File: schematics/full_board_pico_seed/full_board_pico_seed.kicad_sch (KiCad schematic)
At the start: 31 parts, among them J10 Conn_02x20_Odd_Even, J2 Conn_01x02_Male, J9 Conn_01x03, P0 25k, P1 25k, P2 25k, SW4 Enter, SW5 Exit, U12 128X64 OLED Display, U14 AP63205WU, U3 LM1117DT-5.0

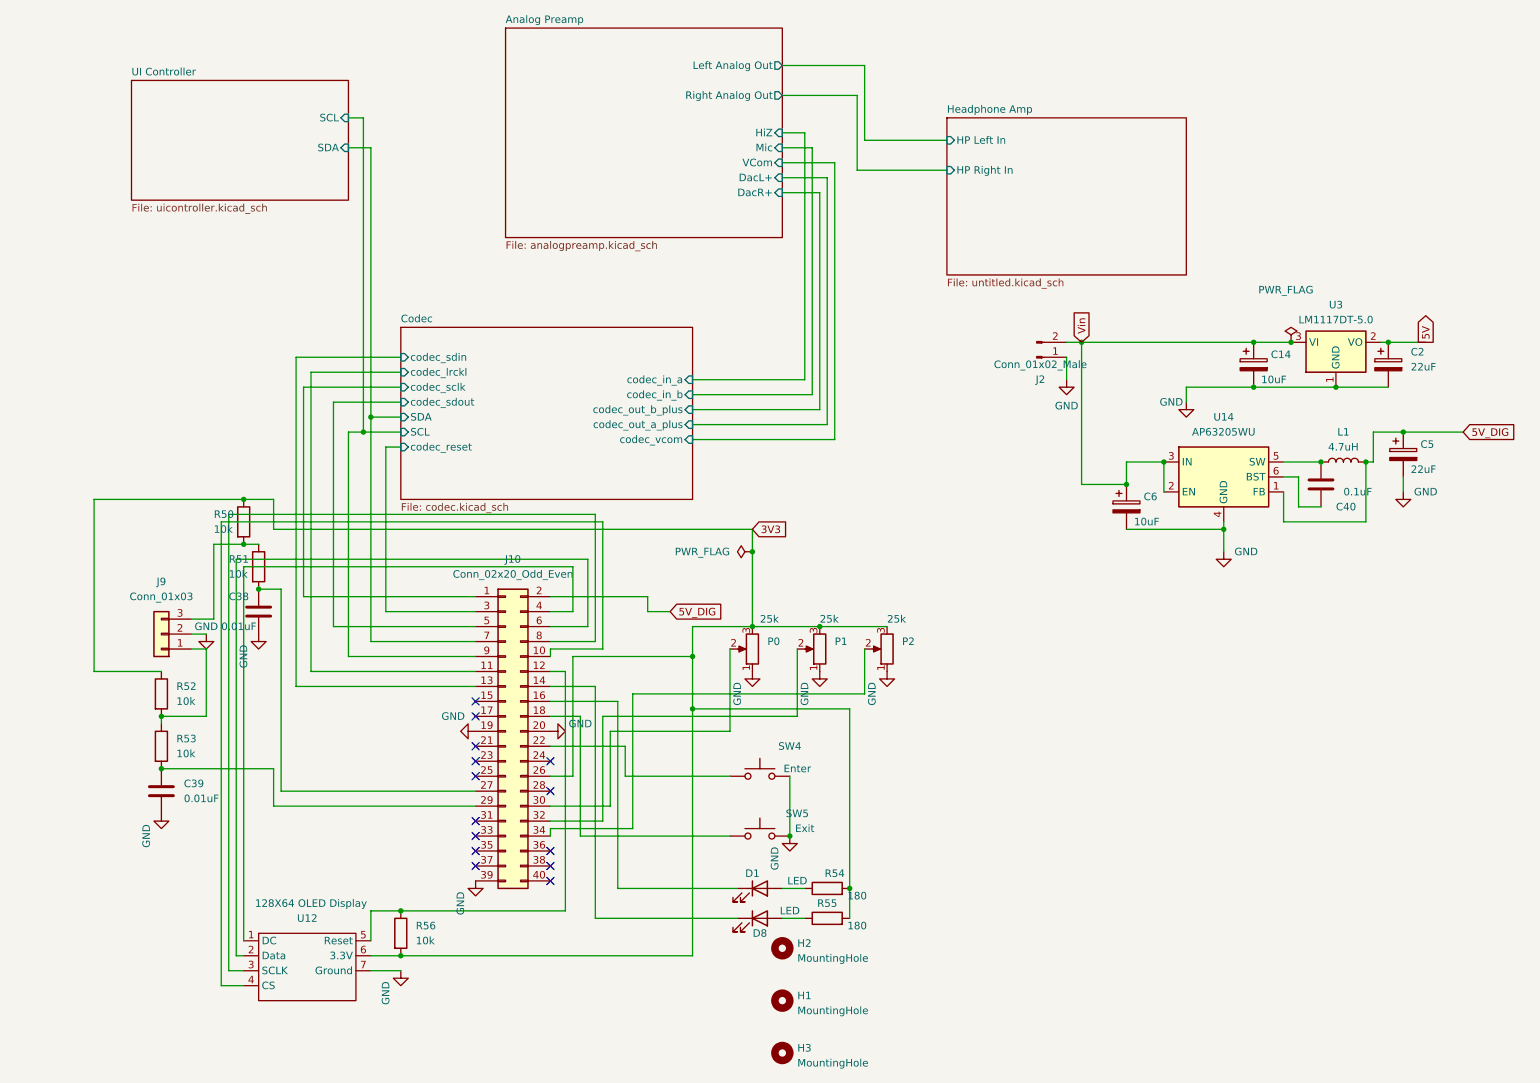
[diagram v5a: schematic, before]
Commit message: corrected schematic regarding pcm3060
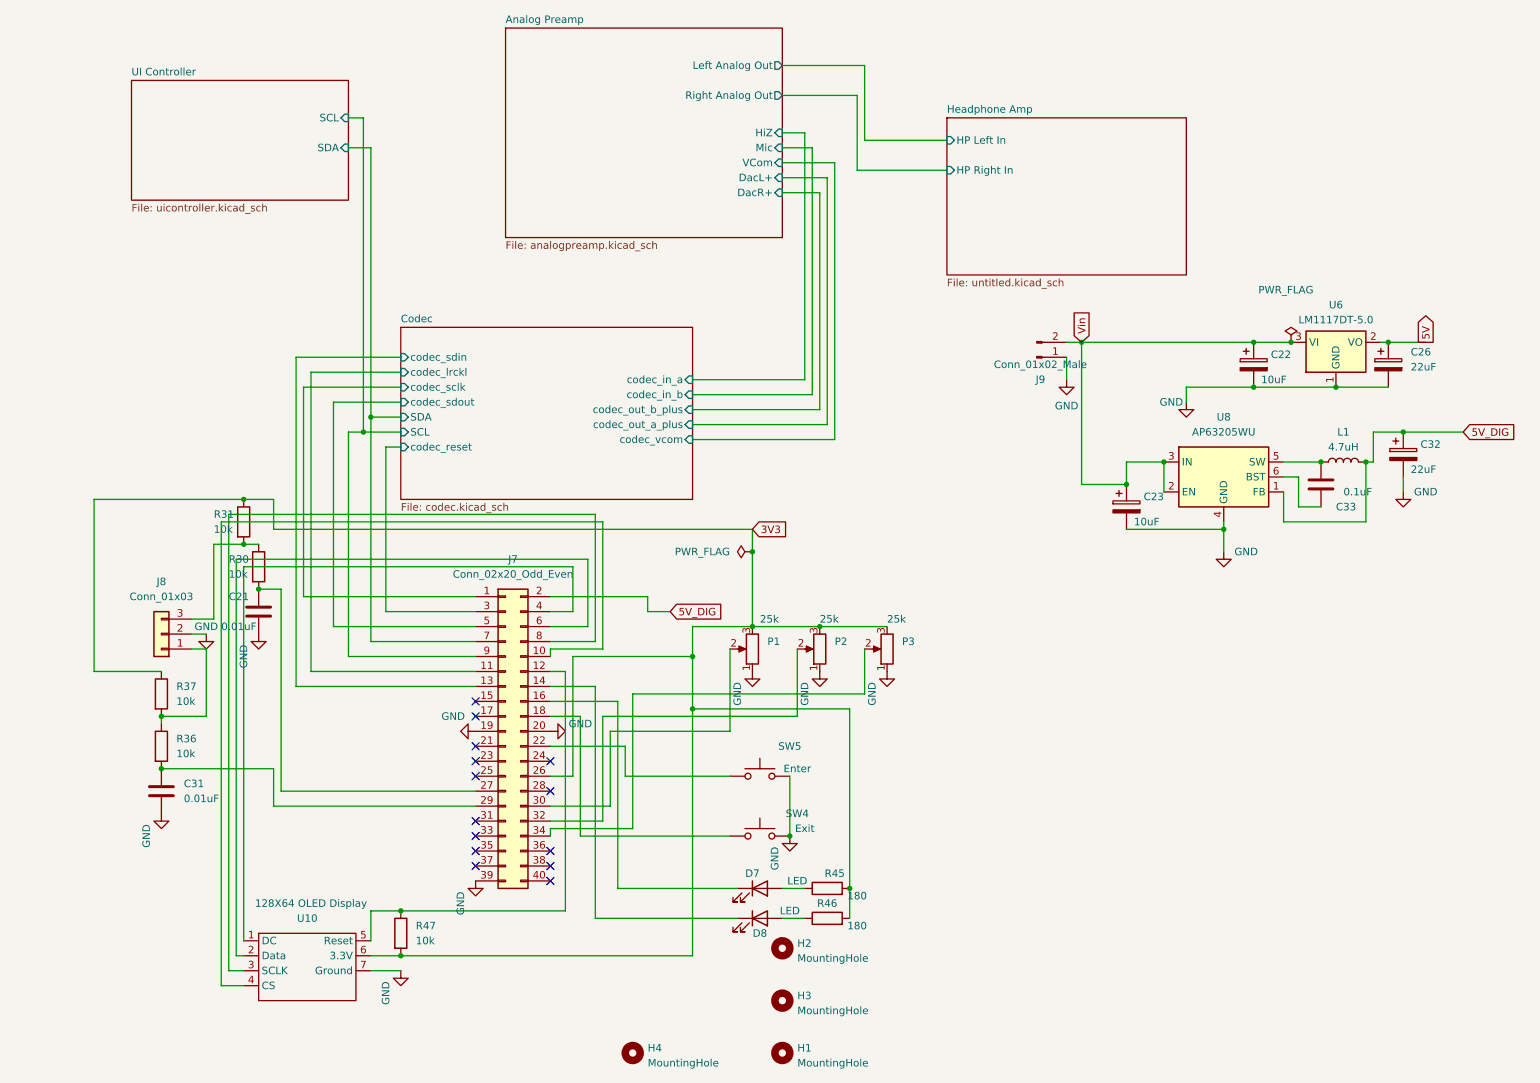
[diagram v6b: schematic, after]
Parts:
- added H4: MountingHole, MountingHole:MountingHole_3.2mm_M3, symbol Mechanical:MountingHole
- renumbered C38 to C21, C14 to C22, C6 to C23, C2 to C26, C39 to C31, C5 to C32, C40 to C33, D1 to D7, H3 to H1, H1 to H3, J10 to J7, J9 to J8, J2 to J9, P0 to P1, P1 to P2, P2 to P3, R51 to R30, R50 to R31, R53 to R36, R52 to R37, R54 to R45, R55 to R46, R56 to R47, SW5 to SW4, SW4 to SW5, U12 to U10, U3 to U6, U14 to U8
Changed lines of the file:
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@@
 	)
 	(symbol
+		(lib_id "Mechanical:MountingHole")
+		(at 132.08 193.04 0)
+		(unit 1)
+		(exclude_from_sim no)
+		(in_bom no)
+		(on_board yes)
+		(dnp no)
+		(fields_autoplaced yes)
+		(property "Reference" "H4"
+			(at 134.62 192.2053 0)
+			(effects
+				(font
+					(size 1.27 1.27)
+				)
+				(justify left)
+			)
+		)
+		(property "Value" "MountingHole"
+			(at 134.62 194.7422 0)
+			(effects
+				(font
+					(size 1.27 1.27)
+				)
+				(justify left)
+			)
+		)
+		(property "Footprint" "MountingHole:MountingHole_3.2mm_M3"
+			(at 132.08 193.04 0)
+			(effects
+				(font
+					(size 1.27 1.27)
+				)
+				(hide yes)
+			)
+		)
+		(property "Datasheet" "~"
+			(at 132.08 193.04 0)
+			(effects
+				(font
+					(size 1.27 1.27)
+				)
+				(hide yes)
+			)
+		)
+		(property "Description" ""
+			(at 132.08 193.04 0)
+			(effects
+				(font
+					(size 1.27 1.27)
+				)
+				(hide yes)
+			)
+		)
+		(instances
+			(project "full_board_pico_seed"
+				(path "/e63e39d7-6ac0-4ffd-8aa3-1841a4541b55"
+					(reference "H4")
+					(unit 1)
+				)
+			)
+		)
+	)
+	(symbol
 		(lib_id "power:GND")
 		(at 105.41 163.83 0)
@@
 		(on_board yes)
 		(dnp no)
-		(property "Reference" "R51"
+		(property "Reference" "R30"
 			(at 63.5 109.22 0)
 			(effects
@@
 			(project "full_board_pico_seed"
 				(path "/e63e39d7-6ac0-4ffd-8aa3-1841a4541b55"
-					(reference "R51")
+					(reference "R30")
 					(unit 1)
 				)
@@
 		(on_board yes)
 		(dnp no)
-		(property "Reference" "P0"
+		(property "Reference" "P1"
 			(at 154.94 123.19 0)
 			(effects
@@
 			(project "full_board_pico_seed"
 				(path "/e63e39d7-6ac0-4ffd-8aa3-1841a4541b55"
-					(reference "P0")
+					(reference "P1")
 					(unit 1)
 				)
@@
 		(dnp no)
 		(fields_autoplaced yes)
-		(property "Reference" "C39"
+		(property "Reference" "C31"
 			(at 55.88 147.32 0)
 			(effects
@@
 			(project "full_board_pico_seed"
 				(path "/e63e39d7-6ac0-4ffd-8aa3-1841a4541b55"
-					(reference "C39")
+					(reference "C31")
 					(unit 1)
 				)
@@
 		(on_board yes)
 		(dnp no)
-		(property "Reference" "P1"
+		(property "Reference" "P2"
 			(at 166.37 123.19 0)
 			(effects
@@
 			(project "full_board_pico_seed"
 				(path "/e63e39d7-6ac0-4ffd-8aa3-1841a4541b55"
-					(reference "P1")
+					(reference "P2")
 					(unit 1)
 				)
@@
 		(dnp no)
 		(fields_autoplaced yes)
-		(property "Reference" "R52"
+		(property "Reference" "R37"
 			(at 54.61 130.81 0)
 			(effects
@@
 			(project "full_board_pico_seed"
 				(path "/e63e39d7-6ac0-4ffd-8aa3-1841a4541b55"
-					(reference "R52")
+					(reference "R37")
 					(unit 1)
 				)
@@
 		(dnp no)
 		(fields_autoplaced yes)
-		(property "Reference" "R56"
+		(property "Reference" "R47"
 			(at 95.25 171.45 0)
 			(effects
@@
 			(project "full_board_pico_seed"
 				(path "/e63e39d7-6ac0-4ffd-8aa3-1841a4541b55"
-					(reference "R56")
+					(reference "R47")
 					(unit 1)
 				)
@@
 		(on_board yes)
 		(dnp no)
-		(property "Reference" "C38"
+		(property "Reference" "C21"
 			(at 63.5 115.57 0)
 			(effects
@@
 			(project "full_board_pico_seed"
 				(path "/e63e39d7-6ac0-4ffd-8aa3-1841a4541b55"
-					(reference "C38")
+					(reference "C21")
 					(unit 1)
 				)
@@
 		(dnp no)
 		(fields_autoplaced yes)
-		(property "Reference" "R53"
+		(property "Reference" "R36"
 			(at 54.61 139.7 0)
 			(effects
@@
 			(project "full_board_pico_seed"
 				(path "/e63e39d7-6ac0-4ffd-8aa3-1841a4541b55"
-					(reference "R53")
+					(reference "R36")
 					(unit 1)
 				)
@@
 		(on_board yes)
 		(dnp no)
-		(property "Reference" "SW5"
+		(property "Reference" "SW4"
 			(at 160.02 152.4 0)
 			(effects
@@
 			(project "full_board_pico_seed"
 				(path "/e63e39d7-6ac0-4ffd-8aa3-1841a4541b55"
-					(reference "SW5")
+					(reference "SW4")
 					(unit 1)
 				)
@@
 		(on_board yes)
 		(dnp no)
-		(property "Reference" "C14"
+		(property "Reference" "C22"
 			(at 240.411 74.4763 0)
 			(effects
@@
 			(project "full_board_pico_seed"
 				(path "/e63e39d7-6ac0-4ffd-8aa3-1841a4541b55"
-					(reference "C14")
+					(reference "C22")
 					(unit 1)
 				)
@@
 		(dnp no)
 		(fields_autoplaced yes)
-		(property "Reference" "H1"
+		(property "Reference" "H3"
 			(at 160.02 183.3153 0)
 			(effects
@@
 			(project "full_board_pico_seed"
 				(path "/e63e39d7-6ac0-4ffd-8aa3-1841a4541b55"
-					(reference "H1")
+					(reference "H3")
 					(unit 1)
 				)
@@
 		(on_board yes)
 		(dnp no)
-		(property "Reference" "C5"
+		(property "Reference" "C32"
 			(at 265.811 89.7163 0)
 			(effects
@@
 			(project "full_board_pico_seed"
 				(path "/e63e39d7-6ac0-4ffd-8aa3-1841a4541b55"
-					(reference "C5")
+					(reference "C32")
 					(unit 1)
 				)
@@
 		(on_board yes)
 		(dnp no)
-		(property "Reference" "J2"
+		(property "Reference" "J9"
 			(at 201.295 78.706 0)
 			(effects
@@
 			(project "full_board_pico_seed"
 				(path "/e63e39d7-6ac0-4ffd-8aa3-1841a4541b55"
-					(reference "J2")
+					(reference "J9")
 					(unit 1)
 				)
@@
 		(dnp no)
 		(fields_autoplaced yes)
-		(property "Reference" "U3"
+		(property "Reference" "U6"
 			(at 251.46 66.04 0)
 			(effects
@@
 			(project "full_board_pico_seed"
 				(path "/e63e39d7-6ac0-4ffd-8aa3-1841a4541b55"
-					(reference "U3")
+					(reference "U6")
 					(unit 1)
 				)
@@
 		(on_board yes)
 		(dnp no)
-		(property "Reference" "R50"
+		(property "Reference" "R31"
 			(at 60.96 101.6 0)
 			(effects
@@
 			(project "full_board_pico_seed"
 				(path "/e63e39d7-6ac0-4ffd-8aa3-1841a4541b55"
-					(reference "R50")
+					(reference "R31")
 					(unit 1)
 				)
@@
 		(on_board yes)
 		(dnp no)
-		(property "Reference" "C40"
+		(property "Reference" "C33"
 			(at 251.46 100.33 0)
 			(effects
@@
 			(project "full_board_pico_seed"
 				(path "/e63e39d7-6ac0-4ffd-8aa3-1841a4541b55"
-					(reference "C40")
+					(reference "C33")
 					(unit 1)
 				)
@@
 		(on_board yes)
 		(dnp no)
-		(property "Reference" "SW4"
+		(property "Reference" "SW5"
 			(at 158.75 140.97 0)
 			(effects
@@
 			(project "full_board_pico_seed"
 				(path "/e63e39d7-6ac0-4ffd-8aa3-1841a4541b55"
-					(reference "SW4")
+					(reference "SW5")
 					(unit 1)
 				)
@@
 		(on_board yes)
 		(dnp no)
-		(property "Reference" "P2"
+		(property "Reference" "P3"
 			(at 177.8 123.19 0)
 			(effects
@@
 			(project "full_board_pico_seed"
 				(path "/e63e39d7-6ac0-4ffd-8aa3-1841a4541b55"
-					(reference "P2")
+					(reference "P3")
 					(unit 1)
 				)
@@
 		(dnp no)
 		(fields_autoplaced yes)
-		(property "Reference" "J10"
+		(property "Reference" "J7"
 			(at 111.76 109.22 0)
 			(effects
@@
 			(project "full_board_pico_seed"
 				(path "/e63e39d7-6ac0-4ffd-8aa3-1841a4541b55"
-					(reference "J10")
+					(reference "J7")
 					(unit 1)
 				)
@@
 		(on_board yes)
 		(dnp no)
-		(property "Reference" "R55"
+		(property "Reference" "R46"
 			(at 165.1 167.64 90)
 			(effects
@@
 			(project "full_board_pico_seed"
 				(path "/e63e39d7-6ac0-4ffd-8aa3-1841a4541b55"
-					(reference "R55")
+					(reference "R46")
 					(unit 1)
 				)
@@
 		(dnp no)
 		(fields_autoplaced yes)
-		(property "Reference" "U14"
+		(property "Reference" "U8"
 			(at 232.41 85.09 0)
 			(effects
@@
 			(project "full_board_pico_seed"
 				(path "/e63e39d7-6ac0-4ffd-8aa3-1841a4541b55"
-					(reference "U14")
+					(reference "U8")
 					(unit 1)
 				)
@@
 		(on_board yes)
 		(dnp no)
-		(property "Reference" "U12"
+		(property "Reference" "U10"
 			(at 76.835 170.18 0)
 			(effects
@@
 			(project "full_board_pico_seed"
 				(path "/e63e39d7-6ac0-4ffd-8aa3-1841a4541b55"
-					(reference "U12")
+					(reference "U10")
 					(unit 1)
 				)
@@
 		(on_board yes)
 		(dnp no)
-		(property "Reference" "R54"
+		(property "Reference" "R45"
 			(at 166.37 162.56 90)
 			(effects
@@
 			(project "full_board_pico_seed"
 				(path "/e63e39d7-6ac0-4ffd-8aa3-1841a4541b55"
-					(reference "R54")
+					(reference "R45")
 					(unit 1)
 				)
@@
 		(dnp no)
 		(fields_autoplaced yes)
-		(property "Reference" "C2"
+		(property "Reference" "C26"
 			(at 264.16 74.0409 0)
 			(effects
@@
 			(project "full_board_pico_seed"
 				(path "/e63e39d7-6ac0-4ffd-8aa3-1841a4541b55"
-					(reference "C2")
+					(reference "C26")
 					(unit 1)
 				)
@@
 		(on_board yes)
 		(dnp no)
-		(property "Reference" "C6"
+		(property "Reference" "C23"
 			(at 218.821 98.6063 0)
 			(effects
@@
 			(project "full_board_pico_seed"
 				(path "/e63e39d7-6ac0-4ffd-8aa3-1841a4541b55"
-					(reference "C6")
+					(reference "C23")
 					(unit 1)
 				)
@@
 		(on_board yes)
 		(dnp no)
-		(property "Reference" "D1"
+		(property "Reference" "D7"
 			(at 152.4 162.56 0)
 			(effects
@@
 			(project "full_board_pico_seed"
 				(path "/e63e39d7-6ac0-4ffd-8aa3-1841a4541b55"
-					(reference "D1")
+					(reference "D7")
 					(unit 1)
 				)
@@
 		(dnp no)
 		(fields_autoplaced yes)
-		(property "Reference" "H3"
+		(property "Reference" "H1"
 			(at 160.02 192.2053 0)
 			(effects
@@
 			(project "full_board_pico_seed"
 				(path "/e63e39d7-6ac0-4ffd-8aa3-1841a4541b55"
-					(reference "H3")
+					(reference "H1")
 					(unit 1)
 				)
@@
 		(dnp no)
 		(fields_autoplaced yes)
-		(property "Reference" "J9"
+		(property "Reference" "J8"
 			(at 52.07 113.03 0)
 			(effects
@@
 			(project "full_board_pico_seed"
 				(path "/e63e39d7-6ac0-4ffd-8aa3-1841a4541b55"
-					(reference "J9")
+					(reference "J8")
 					(unit 1)
 				)
